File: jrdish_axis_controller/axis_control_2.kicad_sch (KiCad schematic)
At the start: 25 parts, among them CN1 KF2EDGR-2.54-9P, CN2 KF2EDGR-2.54-6P

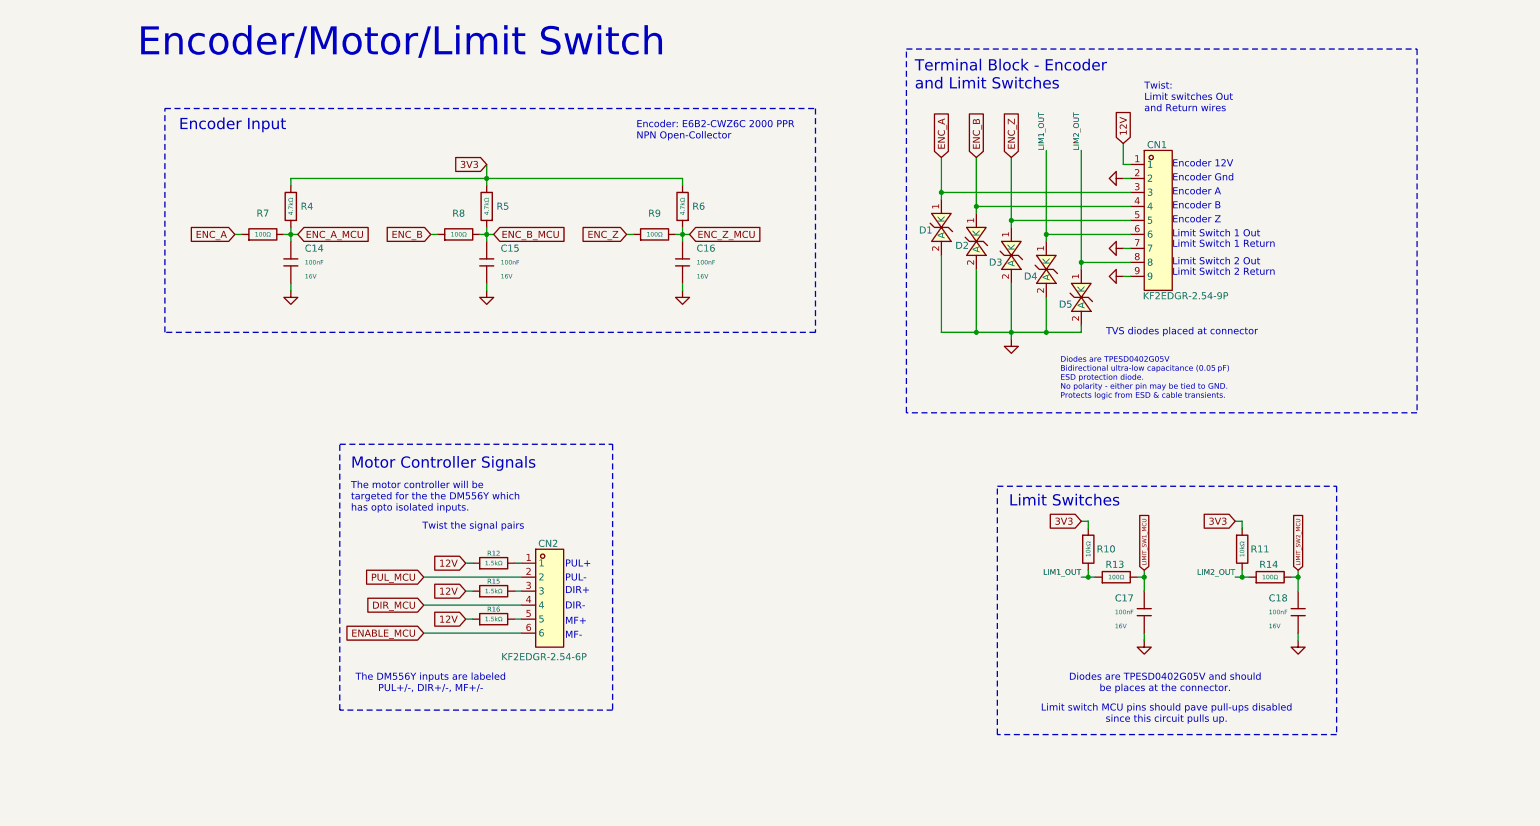
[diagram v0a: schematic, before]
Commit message: New 64pin version - 2 axes
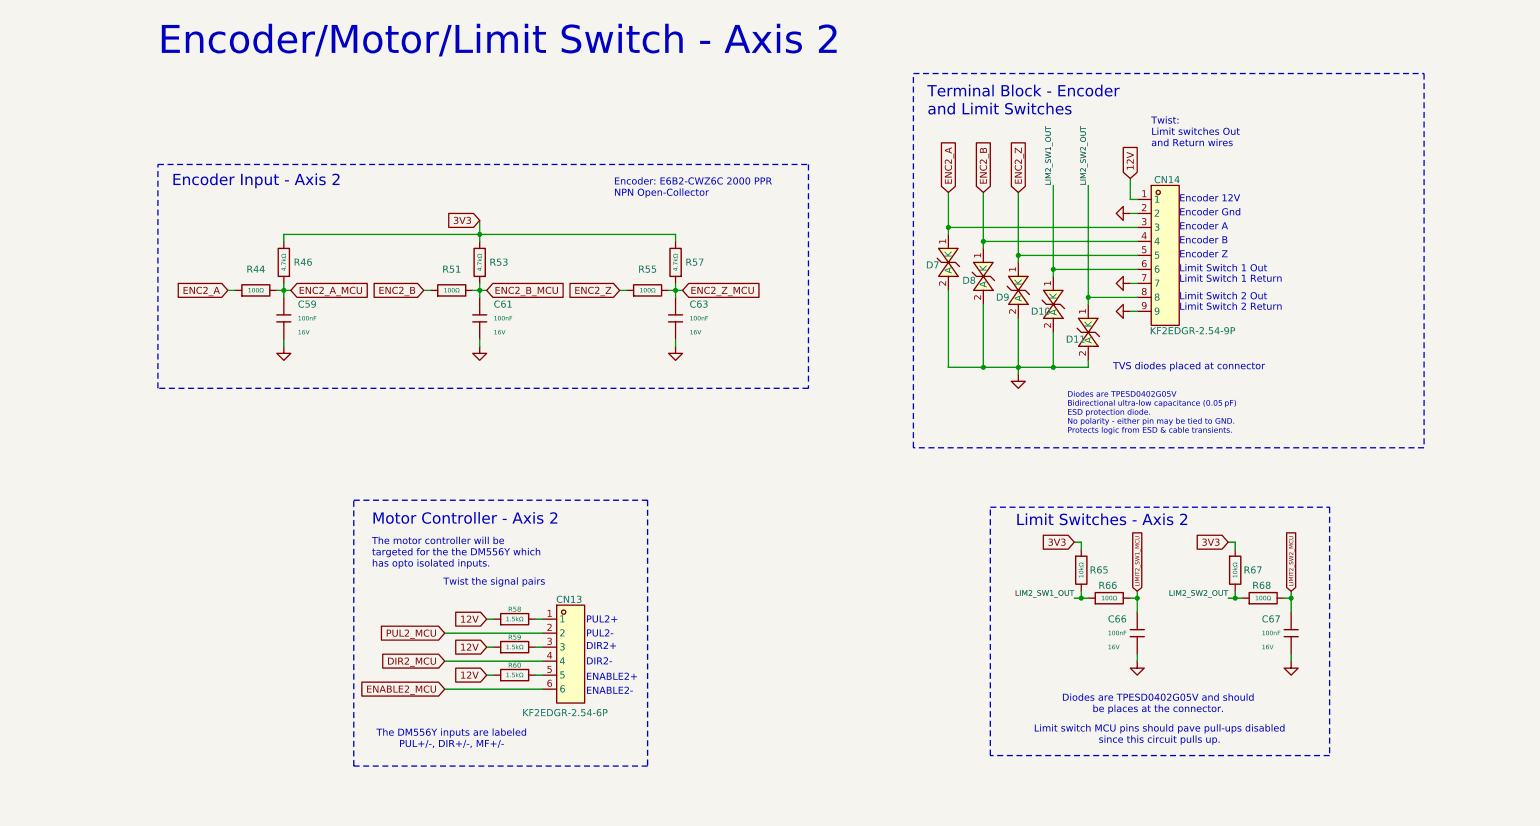
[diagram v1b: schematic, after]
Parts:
- removed C14, C15, C16, C17, C18: 100nF, PCM_JLCPCB:C_0402, symbol PCM_JLCPCB-Capacitors:0402,100nF
- removed CN2: KF2EDGR-2.54-6P, MyParts:CONN-TH_KF2EDGR-2.54-6P, symbol MyParts:KF2EDGR-2.54-6P
- removed R10, R11: 10kΩ, PCM_JLCPCB:R_0402, symbol PCM_JLCPCB-Resistors:0402,10kΩ
- removed R12, R15, R16: 1.5kΩ, PCM_JLCPCB:R_0402, symbol PCM_JLCPCB-Resistors:0402,1.5kΩ
- removed R13, R14, R7, R8, R9: 100Ω, PCM_JLCPCB:R_0402, symbol PCM_JLCPCB-Resistors:0402,100Ω
- removed R4, R5, R6: 4.7kΩ, PCM_JLCPCB:R_0402, symbol PCM_JLCPCB-Resistors:0402,4.7kΩ
- added C59, C61, C63, C66, C67: 100nF, PCM_JLCPCB:C_0402, symbol PCM_JLCPCB-Capacitors:0402,100nF
- added CN13: KF2EDGR-2.54-6P, MyParts:CONN-TH_KF2EDGR-2.54-6P, symbol MyParts:KF2EDGR-2.54-6P
- added R44, R51, R55, R66, R68: 100Ω, PCM_JLCPCB:R_0402, symbol PCM_JLCPCB-Resistors:0402,100Ω
- added R46, R53, R57: 4.7kΩ, PCM_JLCPCB:R_0402, symbol PCM_JLCPCB-Resistors:0402,4.7kΩ
- added R58, R59, R60: 1.5kΩ, PCM_JLCPCB:R_0402, symbol PCM_JLCPCB-Resistors:0402,1.5kΩ
- added R65, R67: 10kΩ, PCM_JLCPCB:R_0402, symbol PCM_JLCPCB-Resistors:0402,10kΩ
- renumbered CN1 to CN14, D4 to D10, D5 to D11, D1 to D7, D2 to D8, D3 to D9
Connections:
- net 12V: now also R58.1, R59.1, R60.1
- net 3V3: now also R46.2, R53.2, R57.2, R65.1, R67.1
- net GND: now also C59.2, C61.2, C63.2, C66.2, C67.2
- net ENC_A renamed ENC2_A
- net ENC2_A: now also R44.1
- net ENC_B renamed ENC2_B
- net ENC2_B: now also R51.1
- net ENC_Z renamed ENC2_Z
- net ENC2_Z: now also R55.1
- net LIM1_OUT renamed LIM2_SW1_OUT
- net LIM2_SW1_OUT: now also R65.2, R66.1
- net LIM2_OUT renamed LIM2_SW2_OUT
- net LIM2_SW2_OUT: now also R67.2, R68.1
- new net: CN13.1, R58.2
- new net: CN13.3, R59.2
- new net: CN13.5, R60.2
- new net DIR2_MCU: CN13.4
- new net ENABLE2_MCU: CN13.6
- new net ENC2_A_MCU: C59.1, R44.2, R46.1
- new net ENC2_B_MCU: C61.1, R51.2, R53.1
- new net ENC2_Z_MCU: C63.1, R55.2, R57.1
- new net LIMIT2_SW1_MCU: C66.1, R66.2
- new net LIMIT2_SW2_MCU: C67.1, R68.2
- new net PUL2_MCU: CN13.2
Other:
- note added: "DIR2+"
- note added: "DIR2-"
- note added: "ENABLE2+"
- note added: "ENABLE2-"
- note added: "Encoder Input - Axis 2"
- note added: "Encoder/Motor/Limit Switch - Axis 2"
- note added: "Limit Switches - Axis 2"
- note added: "Motor Controller - Axis 2"
- note added: "PUL2+"
- note added: "PUL2-"
- note removed: "DIR+"
- note removed: "DIR-"
- note removed: "Encoder Input"
- note removed: "Encoder/Motor/Limit Switch"
- note removed: "Limit Switches"
- note removed: "MF+"
- note removed: "MF-"
- note removed: "Motor Controller Signals"
- note removed: "PUL+"
- note removed: "PUL-"
- moved on the sheet: CN14, D10, D11, D7, D8, D9

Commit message: Continuing layout
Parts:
- removed CN14: KF2EDGR-2.54-9P, MyParts:CONN-TH_9P-P2.54_KF2EDGR-2.54-9P, symbol MyParts:KF2EDGR-2.54-9P
- removed R58, R59, R60: 1.5kΩ, PCM_JLCPCB:R_0402, symbol PCM_JLCPCB-Resistors:0402,1.5kΩ
- added CN3: KF2EDGR-2.54-9P, MyParts:CONN-TH_9P-P2.54_KF2EDGR-2.54-9P, symbol MyParts:KF2EDGR-2.54-9P
- added R41, R42, R43: 330Ω, PCM_JLCPCB:R_0402, symbol PCM_JLCPCB-Resistors:0402,330Ω
- renumbered C59 to C62, C61 to C63, C63 to C64, C66 to C65, C67 to C66, CN13 to CN4, R46 to R31, R53 to R32, R57 to R33, R44 to R34, R51 to R35, R55 to R36, R65 to R37, R67 to R38, R66 to R39, R68 to R40
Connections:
- net 12V: now also CN3.1
- net 3V3: now also R41.1, R42.1, R43.1
- net ENC2_A: now also CN3.3
- net ENC2_B: now also CN3.4
- net ENC2_Z: now also CN3.5
- net GND: now also CN3.2, CN3.7, CN3.9
- net LIM2_SW1_OUT: now also CN3.6
- net LIM2_SW2_OUT: now also CN3.8
- net at CN4.1: now also R41.2
- net at CN4.3: now also R42.2
- net at CN4.5: now also R43.2

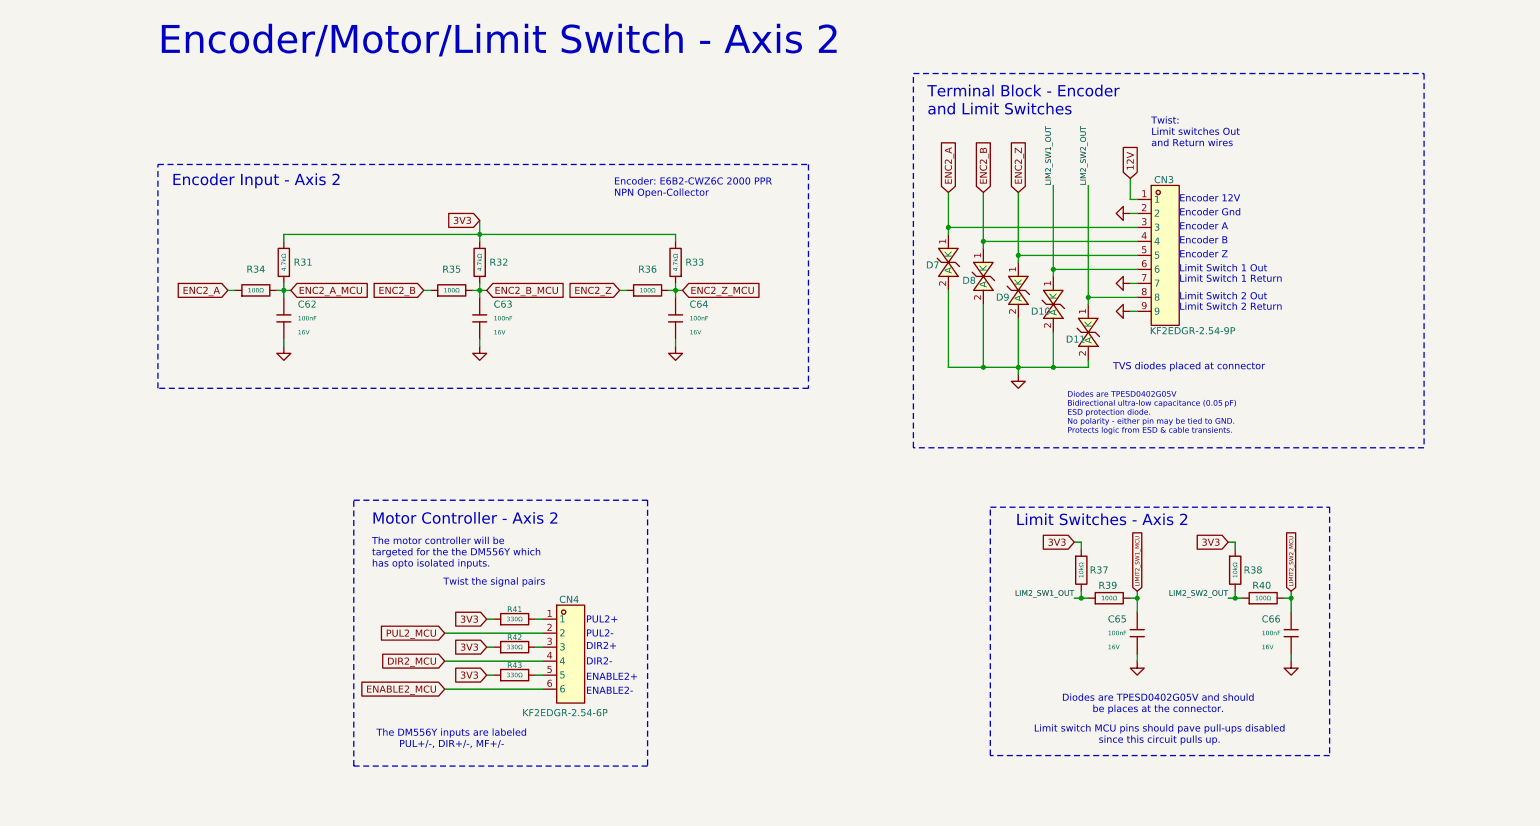
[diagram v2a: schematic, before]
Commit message: RS485 isolated areas in place
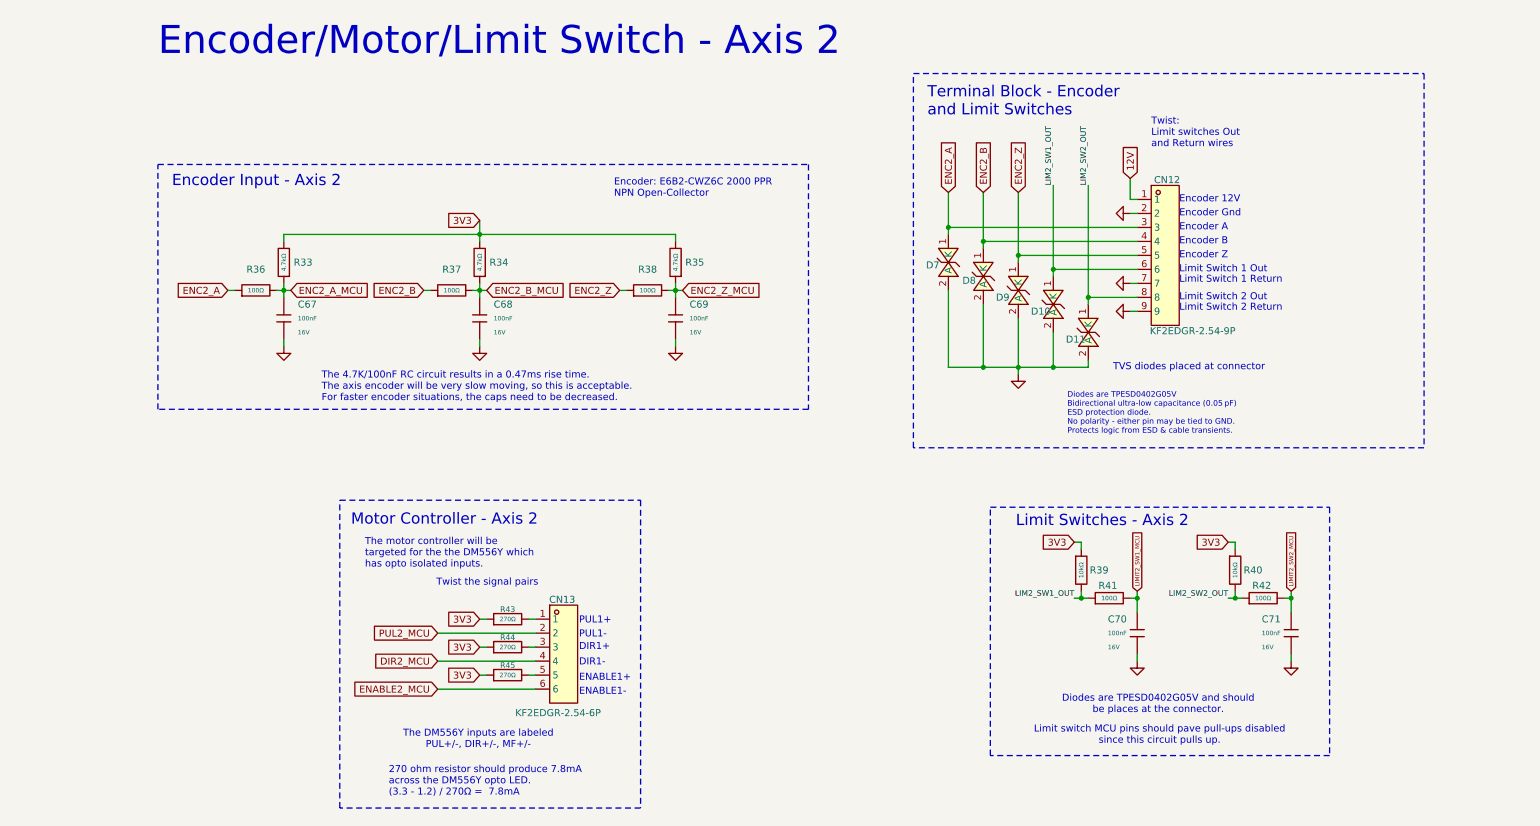
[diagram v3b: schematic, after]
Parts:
- removed CN4: KF2EDGR-2.54-6P, MyParts:CONN-TH_KF2EDGR-2.54-6P, symbol MyParts:KF2EDGR-2.54-6P
- removed R41, R42, R43: 330Ω, PCM_JLCPCB:R_0402, symbol PCM_JLCPCB-Resistors:0402,330Ω
- added CN13: KF2EDGR-2.54-6P, MyParts:CONN-TH_KF2EDGR-2.54-6P, symbol MyParts:KF2EDGR-2.54-6P
- added R43, R44, R45: 270Ω, PCM_JLCPCB:R_0603, symbol PCM_JLCPCB-Resistors:0603,270Ω
- renumbered C62 to C67, C63 to C68, C64 to C69, C65 to C70, C66 to C71, CN3 to CN12, R31 to R33, R32 to R34, R33 to R35, R34 to R36, R35 to R37, R36 to R38, R37 to R39, R38 to R40, R39 to R41, R40 to R42
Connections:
- net 3V3: now also R43.1, R44.1, R45.1
- net DIR2_MCU: now also CN13.4
- net ENABLE2_MCU: now also CN13.6
- net PUL2_MCU: now also CN13.2
- new net: CN13.1, R43.2
- new net: CN13.3, R44.2
- new net: CN13.5, R45.2
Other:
- note added: "270 ohm resistor should produce 7.8mA across the DM556Y opto LED. (3.3 - 1.2) / 270Ω = 7.8mA"
- note added: "DIR1+"
- note added: "DIR1-"
- note added: "ENABLE1+"
- note added: "ENABLE1-"
- note added: "PUL1+"
- note added: "PUL1-"
- note added: "The 4.7K/100nF RC circuit results in a 0.47ms rise time. The axis encoder will be very slow moving, so this is acceptable. For faster encoder situations, the caps need to be decreased."
- note removed: "DIR2+"
- note removed: "DIR2-"
- note removed: "ENABLE2+"
- note removed: "ENABLE2-"
- note removed: "PUL2+"
- note removed: "PUL2-"

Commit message: Layout complete
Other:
- note added: "Diodes are TPESD0402G05V Bidirectional ultra-low capacitance (0.05 pF) ESD protection diode. No polarity - either pin may be tied to GND. Protects logic from ESD & cable transients. Encoder is the E6B2-CWZ6C NPN Open-collector Output Model."
- note removed: "Diodes are TPESD0402G05V Bidirectional ultra-low capacitance (0.05 pF) ESD protection diode. No polarity - either pin may be tied to GND. Protects logic from ESD & cable transients."
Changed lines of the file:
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@@
 		)
 	)
-	(text "Diodes are TPESD0402G05V\nBidirectional ultra-low capacitance (0.05 pF) \nESD protection diode.\nNo polarity - either pin may be tied to GND.\nProtects logic from ESD & cable transients."
+	(text "Diodes are TPESD0402G05V\nBidirectional ultra-low capacitance (0.05 pF) \nESD protection diode.\nNo polarity - either pin may be tied to GND.\nProtects logic from ESD & cable transients.\nEncoder is the E6B2-CWZ6C NPN Open-collector Output Model."
 		(exclude_from_sim no)
 		(at 191.77 87.122 0)
@@
 	)
 	(symbol
+		(lib_name "TPESD0402G05V_4")
 		(lib_id "MyParts:TPESD0402G05V")
 		(at 189.23 67.31 270)
@@
 			)
 		)
-		(property "Datasheet" ""
+		(property "Datasheet" "https://www.lcsc.com/datasheet/C558615.pdf?spm=wm.sxq.inf.ggs___wm.ssy.bg.0.xh&lcsc_vid=FFBaV1wHQFldUVICFgBfBVJTQVJWXgBfEQRYBAFQE1YxVlNRQFVXU1JRQVReUTsOAxUeFF5JWBYZEEoKFBINSQcJGk4eFQsCAgIaSgADAwAHC0slRldcU1ZUWQkaCgg%3D"
 			(at 189.23 67.31 0)
 			(hide yes)
@@
 			)
 		)
-		(property "Description" ""
+		(property "Description" "5VWM 40VC 0402"
 			(at 189.23 67.31 0)
+			(hide yes)
 			(show_name no)
 			(do_not_autoplace no)
@@
 	)
 	(symbol
+		(lib_name "TPESD0402G05V_3")
 		(lib_id "MyParts:TPESD0402G05V")
 		(at 182.88 64.77 270)
@@
 			)
 		)
-		(property "Datasheet" ""
+		(property "Datasheet" "https://www.lcsc.com/datasheet/C558615.pdf?spm=wm.sxq.inf.ggs___wm.ssy.bg.0.xh&lcsc_vid=FFBaV1wHQFldUVICFgBfBVJTQVJWXgBfEQRYBAFQE1YxVlNRQFVXU1JRQVReUTsOAxUeFF5JWBYZEEoKFBINSQcJGk4eFQsCAgIaSgADAwAHC0slRldcU1ZUWQkaCgg%3D"
 			(at 182.88 64.77 0)
 			(hide yes)
@@
 			)
 		)
-		(property "Description" ""
+		(property "Description" "5VWM 40VC 0402"
 			(at 182.88 64.77 0)
+			(hide yes)
 			(show_name no)
 			(do_not_autoplace no)
@@
 	)
 	(symbol
+		(lib_name "TPESD0402G05V_2")
 		(lib_id "MyParts:TPESD0402G05V")
 		(at 176.53 62.23 270)
@@
 			)
 		)
-		(property "Datasheet" ""
+		(property "Datasheet" "https://www.lcsc.com/datasheet/C558615.pdf?spm=wm.sxq.inf.ggs___wm.ssy.bg.0.xh&lcsc_vid=FFBaV1wHQFldUVICFgBfBVJTQVJWXgBfEQRYBAFQE1YxVlNRQFVXU1JRQVReUTsOAxUeFF5JWBYZEEoKFBINSQcJGk4eFQsCAgIaSgADAwAHC0slRldcU1ZUWQkaCgg%3D"
 			(at 176.53 62.23 0)
 			(hide yes)
@@
 			)
 		)
-		(property "Description" ""
+		(property "Description" "5VWM 40VC 0402"
 			(at 176.53 62.23 0)
+			(hide yes)
 			(show_name no)
 			(do_not_autoplace no)
@@
 			)
 		)
-		(property "Datasheet" ""
+		(property "Datasheet" "https://www.lcsc.com/datasheet/C558615.pdf?spm=wm.sxq.inf.ggs___wm.ssy.bg.0.xh&lcsc_vid=FFBaV1wHQFldUVICFgBfBVJTQVJWXgBfEQRYBAFQE1YxVlNRQFVXU1JRQVReUTsOAxUeFF5JWBYZEEoKFBINSQcJGk4eFQsCAgIaSgADAwAHC0slRldcU1ZUWQkaCgg%3D"
 			(at 195.58 72.39 0)
 			(hide yes)
@@
 			)
 		)
-		(property "Description" ""
+		(property "Description" "5VWM 40VC 0402"
 			(at 195.58 72.39 0)
+			(hide yes)
 			(show_name no)
 			(do_not_autoplace no)
@@
 	)
 	(symbol
+		(lib_name "TPESD0402G05V_1")
 		(lib_id "MyParts:TPESD0402G05V")
 		(at 170.18 59.69 270)
@@
 			)
 		)
-		(property "Datasheet" ""
+		(property "Datasheet" "https://www.lcsc.com/datasheet/C558615.pdf?spm=wm.sxq.inf.ggs___wm.ssy.bg.0.xh&lcsc_vid=FFBaV1wHQFldUVICFgBfBVJTQVJWXgBfEQRYBAFQE1YxVlNRQFVXU1JRQVReUTsOAxUeFF5JWBYZEEoKFBINSQcJGk4eFQsCAgIaSgADAwAHC0slRldcU1ZUWQkaCgg%3D"
 			(at 170.18 59.69 0)
 			(hide yes)
@@
 			)
 		)
-		(property "Description" ""
+		(property "Description" "5VWM 40VC 0402"
 			(at 170.18 59.69 0)
+			(hide yes)
 			(show_name no)
 			(do_not_autoplace no)

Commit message: Making refinements
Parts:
- added D21, D22, D23: TPESD0402G05V, MyParts:D0402-BI, symbol MyParts:TPESD0402G05V
- added R60, R61, R62: 100Ω, PCM_JLCPCB:R_0402, symbol PCM_JLCPCB-Resistors:0402,100Ω
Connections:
- net DIR2_MCU: now also R61.1; no longer CN13.4
- net ENABLE2_MCU: now also R62.1; no longer CN13.6
- net GND: now also D21.2 (A), D22.2 (A), D23.2 (A)
- net PUL2_MCU: now also R60.1; no longer CN13.2
- new net: CN13.4, D22.1 (K), R61.2
- new net: CN13.2, D21.1 (K), R60.2
- new net: CN13.6, D23.1 (K), R62.2

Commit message: Making refinements
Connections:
- removed net GND: C67.2, C68.2, C69.2, C70.2, C71.2, CN12.2, CN12.7, CN12.9, D10.2 (A), D11.2 (A), D21.2 (A), D22.2 (A), D23.2 (A), D7.2 (A), D8.2 (A), D9.2 (A)
- new net: D10.2 (A), D11.2 (A), D7.2 (A), D8.2 (A), D9.2 (A)
- new net: D21.2 (A), D22.2 (A), D23.2 (A)
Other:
- note added: "DIR2+"
- note added: "DIR2-"
- note added: "ENABLE2+"
- note added: "ENABLE2-"
- note added: "PUL2+"
- note added: "PUL2-"
- note removed: "DIR1+"
- note removed: "DIR1-"
- note removed: "ENABLE1+"
- note removed: "ENABLE1-"
- note removed: "PUL1+"
- note removed: "PUL1-"
- title: Encoder/Motor/Limit Switch -> Encoder/Motor/Limit Switch - Axis2
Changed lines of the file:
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@@
 	(paper "A4")
 	(title_block
-		(title "Encoder/Motor/Limit Switch")
-		(date "2026-04-12")
+		(title "Encoder/Motor/Limit Switch - Axis2")
+		(date "2026-04-30")
 		(rev "1.0")
 		(company "JRSeti")
@@
 		)
 	)
-	(text "PUL1-"
+	(text "PUL2-"
 		(exclude_from_sim no)
 		(at 103.124 127.254 0)
@@
 		)
 	)
-	(text "DIR1-"
+	(text "DIR2-"
 		(exclude_from_sim no)
 		(at 103.124 132.334 0)
@@
 		)
 	)
-	(text "DIR1+"
+	(text "DIR2+"
 		(exclude_from_sim no)
 		(at 103.124 129.54 0)
@@
 		)
 	)
-	(text "ENABLE1+"
+	(text "ENABLE2+"
 		(exclude_from_sim no)
 		(at 103.124 135.128 0)
@@
 		)
 	)
-	(text "ENABLE1-"
+	(text "ENABLE2-"
 		(exclude_from_sim no)
 		(at 103.124 137.668 0)
@@
 		)
 	)
-	(text "PUL1+"
+	(text "PUL2+"
 		(exclude_from_sim no)
 		(at 103.124 124.714 0)
